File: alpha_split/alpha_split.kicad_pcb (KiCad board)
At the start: 2 copper layers, 109 x 71 mm, 154 parts, among them J1 USB_C_Receptacle, J2 USB_C_Receptacle, J3 PDI, J4 D4, J5 D5, J6 A6, J7 A7, J8 B0, J9 E2, K00 K00, K01 K01, K02 K02, K03 K03, K04 K04, K05 K05, K10 K10, K11 K11, K12 K12, K13 K13, K14 K14, K15 K15, K20 K20, K21 K21, K22 K22, K23 K23, K24 K24, K25 K25, K30 K30, K31 K31, K32 K32, K33 K33, K34 K34, K35 K35, SW1 Switch-6P-2S2T, SW2 RST_SW, U1 MCP73831, U2 MCP1700 (3.0V), U3 MCP1700 (3.3V), U4 ATXMEGA-A4U-EPAD, U5 74LVC1G34, U6 nRF24L01_module, U7 FSUSB42, U8 FSUSB42, U9 FSUSB42

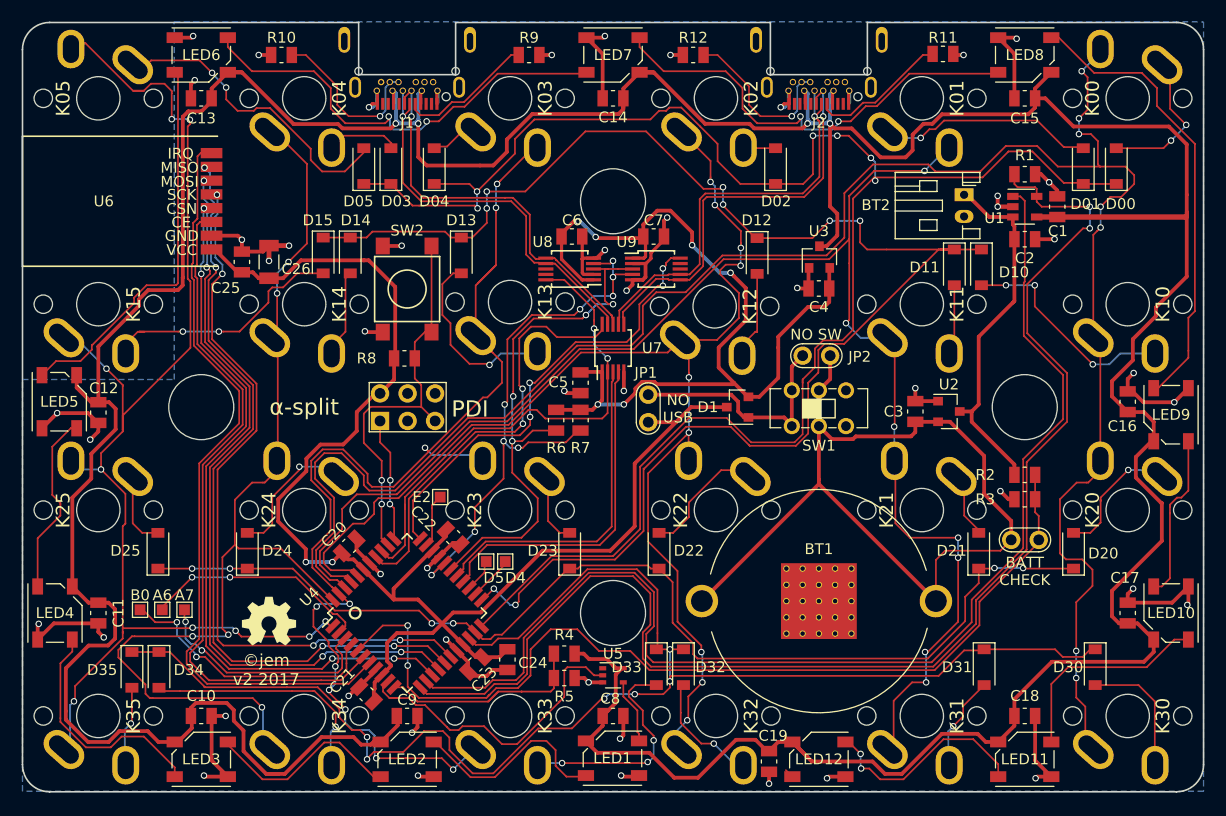
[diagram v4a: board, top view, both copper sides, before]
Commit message: updates for alpha split based on v2 prototype board
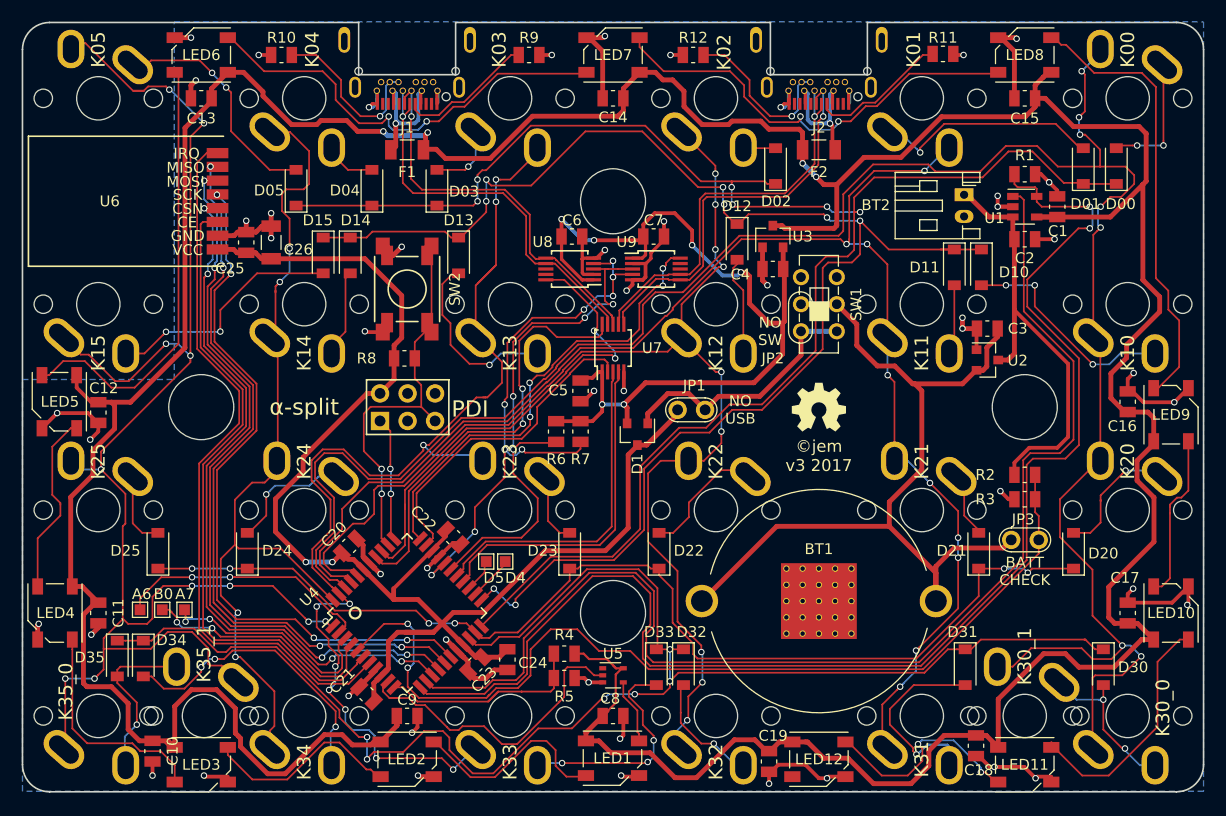
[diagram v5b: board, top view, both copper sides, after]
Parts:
- removed J9: E2, TestPoint:TestPoint_Pad_1.0x1.0mm
- added F1: Polyfuse, Resistor_SMD:R_1206_3216Metric, F.Cu at (35.5, 11.8)
- added F2: Polyfuse, Resistor_SMD:R_1206_3216Metric, F.Cu at (73.5, 11.8)
- added K30_1: K31, switch_mx:Cherry_MX_Matias_Slots_NoSilk_Back, B.Cu at (92.5, 64.0)
- added K35_1: K35, switch_mx:Cherry_MX_Matias_Slots_NoSilk_Back, B.Cu at (16.8, 64.0)
- SW2: value RST_SW -> SW_Push; footprint switch:SwitchPush_C&K_PTS645_SMT -> switch:SwitchPush_C&K_MultiFoot_RS-187R05A2-DS_And_PTS645_SMT
- moved svg2mod 54.5 mm to (73.5, 35.5)
- moved C3 10.1 mm to (89.0, 28.2), turned to 0 degrees
- moved SW1 9.60 mm to (73.5, 26.0), turned to 90 degrees
- moved D1 9.58 mm to (56.8, 38.0), turned to 270 degrees
- moved D05 6.56 mm to (25.2, 15.2)
- moved U2 5.93 mm to (89.0, 31.1)
- moved C10 5.55 mm to (12.0, 67.2), turned to 270 degrees
- moved JP1 5.43 mm to (63.0, 35.8), turned to 270 degrees
- moved C18 5.27 mm to (88.0, 66.8), turned to 270 degrees
- moved U3 4.70 mm to (69.2, 19.8)
- moved C4 4.62 mm to (69.2, 22.8)
- moved JP2 3.55 mm to (71.8, 28.5), turned to 180 degrees
- moved D04 2.66 mm to (32.2, 15.2)
- moved D12 2.26 mm to (66.0, 20.2)
- moved J6 2.05 mm to (10.8, 54.2)
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- renumbered K30 to K30_0, K35 to K35_0
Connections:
- J1 pad : Net-(J1-PadB5) -> (no net)
- J1 pad A4: +5V -> Net-(F1-Pad1)
- J1 pad A9: +5V -> Net-(F1-Pad1)
- J1 pad B4: +5V -> Net-(F1-Pad1)
- J1 pad B5: Net-(J1-PadB5) -> Net-(J1-PadB3)
- J1 pad B9: +5V -> Net-(F1-Pad1)
- J2 pad : Net-(J2-PadB5) -> (no net)
- J2 pad A4: +5V -> Net-(F2-Pad1)
- J2 pad A9: +5V -> Net-(F2-Pad1)
- J2 pad B4: +5V -> Net-(F2-Pad1)
- J2 pad B5: Net-(J2-PadB5) -> Net-(J2-PadB3)
- J2 pad B9: +5V -> Net-(F2-Pad1)
- R10 pad 1: Net-(J1-PadB5) -> Net-(J1-PadB3)
- R12 pad 1: Net-(J2-PadB5) -> Net-(J2-PadB3)
- SW2 pad 2: GND -> /RST
- U4 pad 32: /E2 -> /USB_SEL
- U7 pad 2: /I2C_LEFT -> /USB_SEL
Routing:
- net +5V: track 424.6 -> 278.5 mm, vias 4 -> 15
- net GND: track 173.2 -> 283.8 mm, vias 49 -> 40
- net /USB_SEL: track 0.00 -> 30.3 mm
- net /COL5: track 122.1 -> 147.7 mm, vias 9 -> 11
- net Net-(LED12-Pad2): track 0.85 -> 18.4 mm, vias 0 -> 2
- net Net-(LED10-Pad4): track 15.4 -> 32.5 mm
- net /COL0: track 188.6 -> 205.2 mm
- net Net-(J1-PadB5): track 16.0 -> 0.00 mm, vias 1 -> 0
- net Net-(J1-PadB3): track 0.00 -> 16.0 mm, vias 0 -> 1
- net Net-(J2-PadB5): track 15.8 -> 0.00 mm, vias 1 -> 0
- net Net-(J2-PadB3): track 0.00 -> 15.7 mm, vias 0 -> 1
- net Net-(LED2-Pad2): track 18.5 -> 34.0 mm
- net Net-(LED8-Pad2): track 42.6 -> 27.7 mm, vias 0 -> 1
- net Net-(LED7-Pad2): track 42.3 -> 27.6 mm, vias 2 -> 1
- net /COL4: track 97.5 -> 84.1 mm, vias 6 -> 4
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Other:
- net class Escape removed
- net class Power: trace_width 0.35 -> 0.45
- board text added: "NO SW"
- board text added: "©jem v3 2017"
- board text removed: "E2"
- board text removed: "©jem v2 2017"

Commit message: BAT_PROG signal not connected properly
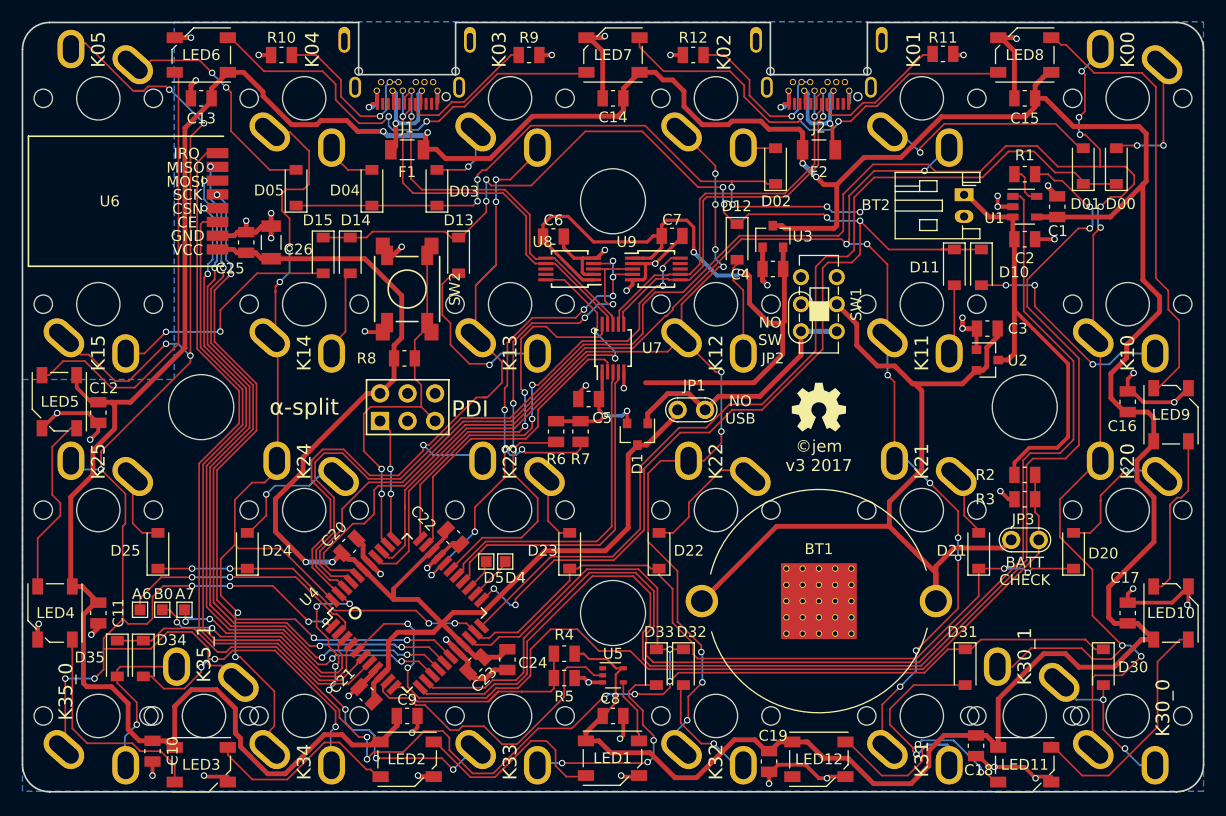
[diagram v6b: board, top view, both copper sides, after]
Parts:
- F1, F2: value Polyfuse -> Fuse
- K30_1: value K31 -> K30
- moved C6 1.70 mm to (49.0, 19.8)
- moved C7 1.70 mm to (60.0, 19.7)
- moved C5 1.06 mm to (52.2, 34.8), turned to 180 degrees
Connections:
- R1 pad 1: /BAT_PROG -> Net-(R1-Pad1)
- R1 pad 2: GND -> /BAT_PROG
- U1 pad 5: /BAT_PROG -> Net-(R1-Pad1)
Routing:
- net GND: track 283.8 -> 166.8 mm, vias 40 -> 51
- net +5V: track 278.5 -> 394.8 mm, vias 15 -> 4
- net Net-(LED12-Pad2): track 18.4 -> 0.00 mm, vias 2 -> 0
- net Net-(LED10-Pad4): track 32.5 -> 15.4 mm
- net Net-(LED2-Pad2): track 34.0 -> 18.7 mm
- net Net-(LED7-Pad2): track 27.6 -> 41.6 mm, vias 1 -> 2
- net Net-(LED8-Pad2): track 27.7 -> 41.4 mm, vias 1 -> 0
- net Net-(LED10-Pad2): track 10.6 -> 22.5 mm
- net Net-(LED3-Pad2): track 10.6 -> 20.6 mm
- net Net-(LED5-Pad2): track 31.8 -> 41.8 mm, vias 1 -> 0
- net Net-(LED6-Pad2): track 46.7 -> 42.3 mm, vias 1 -> 2
- net Net-(R1-Pad1): track 0.00 -> 3.89 mm
- net /BAT_PROG: track 126.0 -> 122.4 mm
- net Net-(LED1-Pad2): track 22.5 -> 19.1 mm
- net Net-(LED11-Pad2): track 21.7 -> 20.3 mm, vias 0 -> 2
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
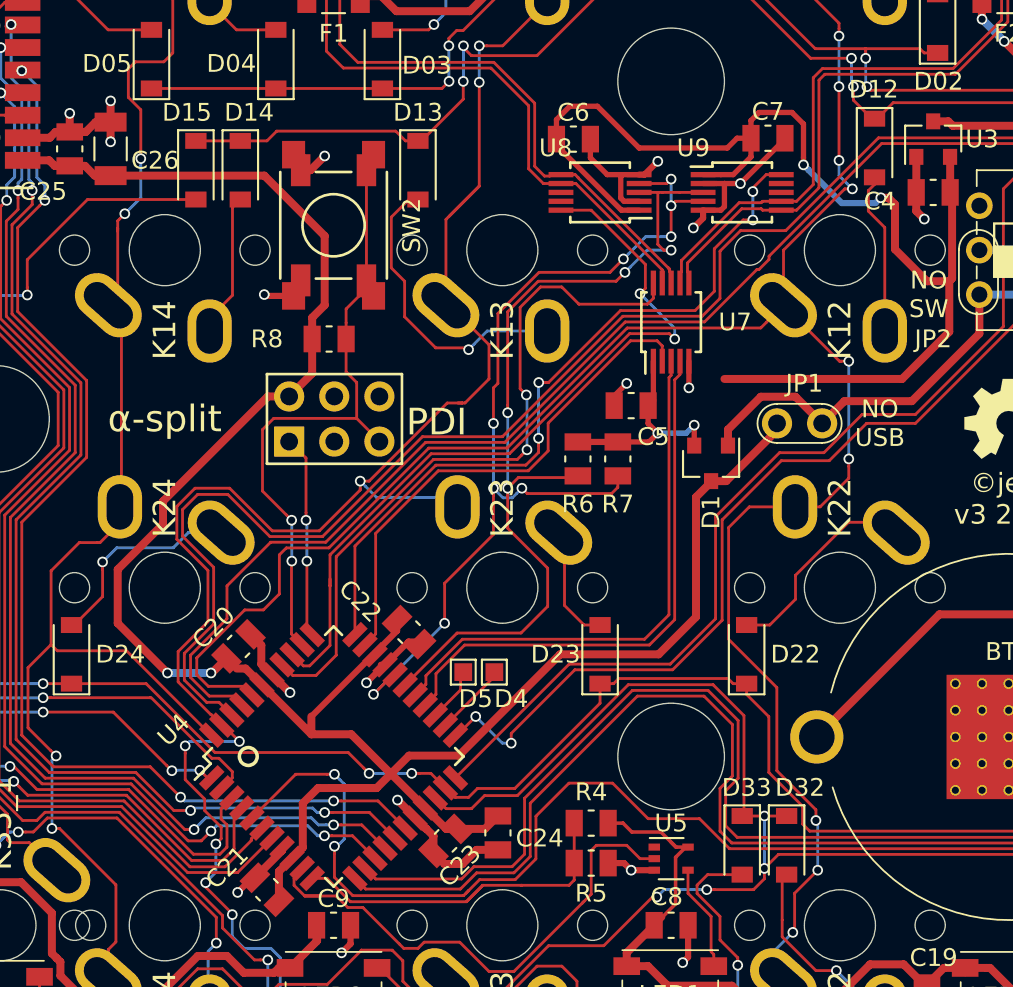
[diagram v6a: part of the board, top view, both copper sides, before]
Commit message: add Tag Connect programming header
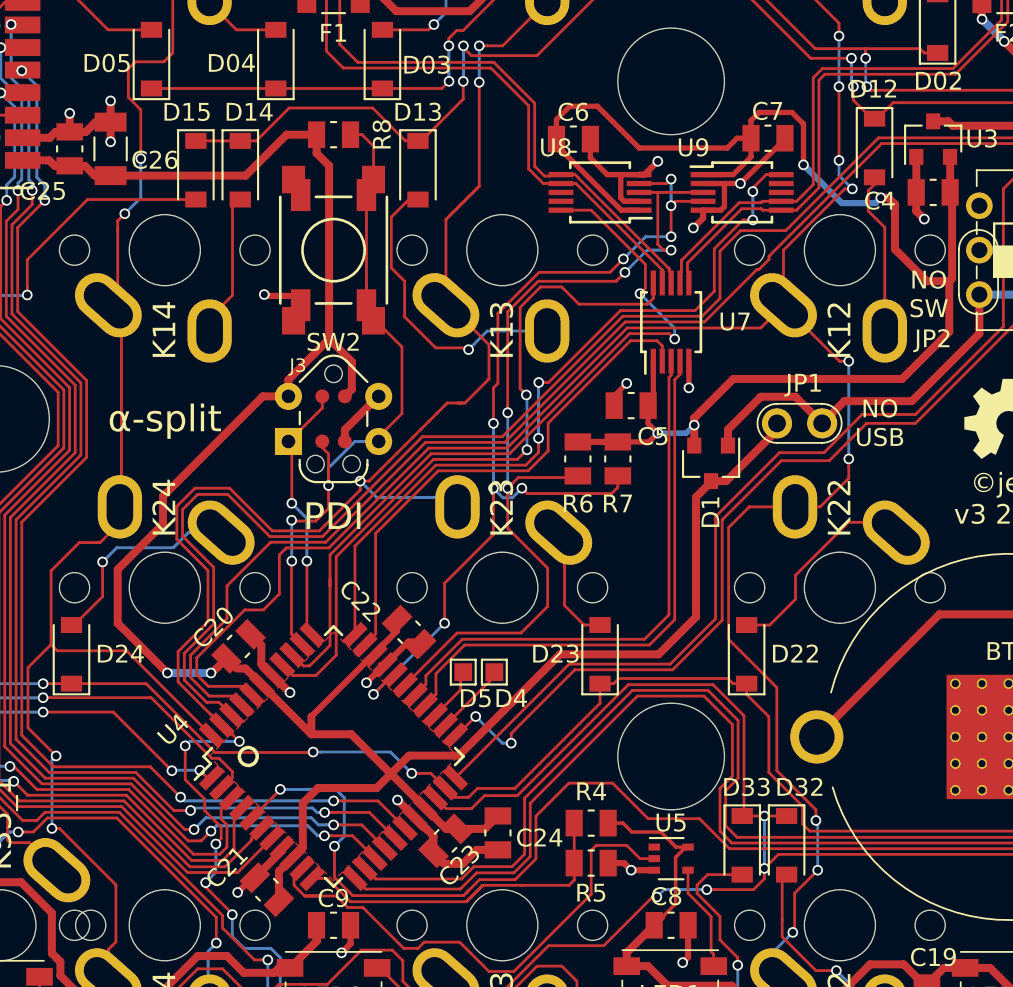
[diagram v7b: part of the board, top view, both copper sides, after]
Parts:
- J3: value PDI -> TC2030-IDC; footprint Conn_PinHeader_2.54mm:PinHeader_2x03_P2.54mm_Vertical -> Tag-Connect:TC2030-NL_SMALL_AND_IDC_PDI
- moved R8 11.5 mm to (35.5, 19.5)
- moved J3 2.81 mm to (35.5, 35.5), turned to 270 degrees
- moved SW2 1.40 mm to (35.5, 26.0)
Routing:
- net VCC: track 135.8 -> 141.1 mm
- net /PDI: track 11.5 -> 14.9 mm
- net +3V3: track 81.3 -> 84.4 mm
- net /RST: track 35.7 -> 38.3 mm, vias 2 -> 3
- net GND: track 166.8 -> 169.1 mm, vias 51 -> 50
- net /BAT_LVL: track 88.9 -> 87.7 mm
- net /ROW1: track 136.1 -> 137.2 mm
- added copper zone on F.Cu, net VCC

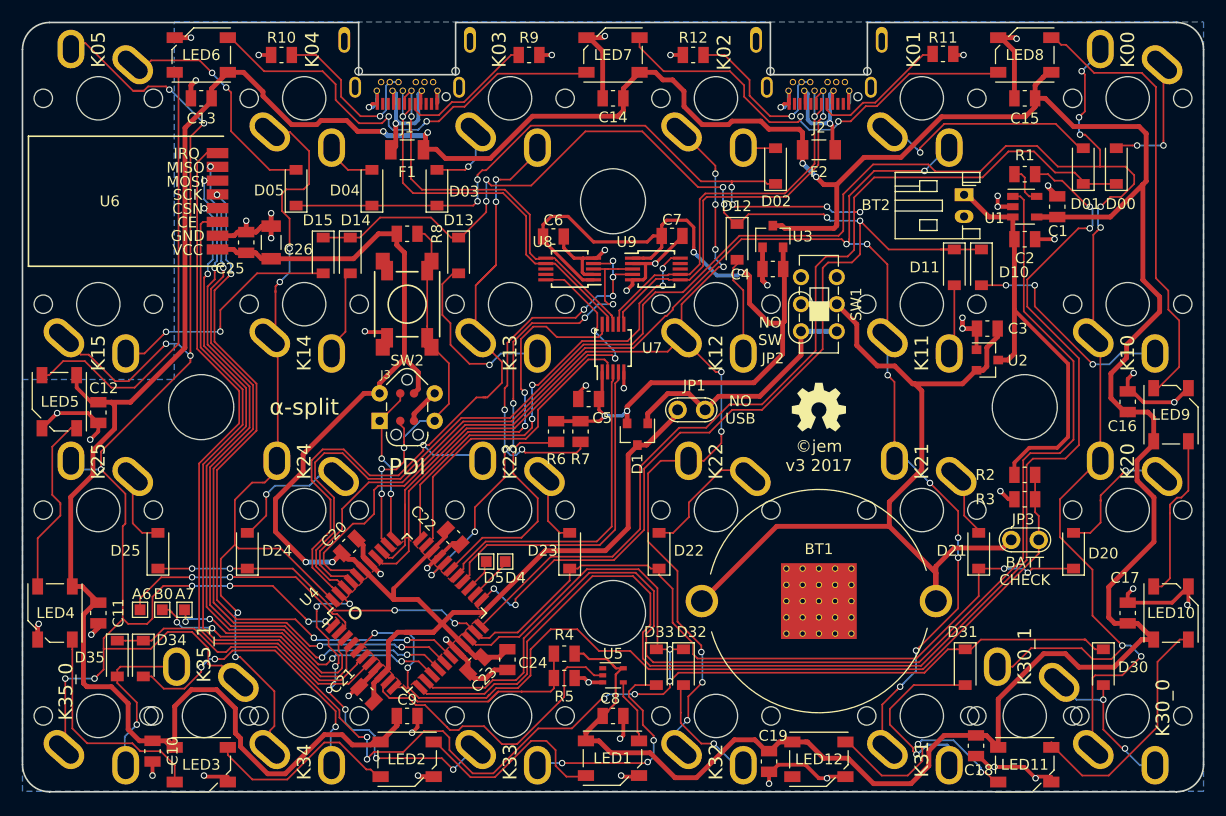
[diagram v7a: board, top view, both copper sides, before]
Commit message: give up on trying to support multiple switch layouts
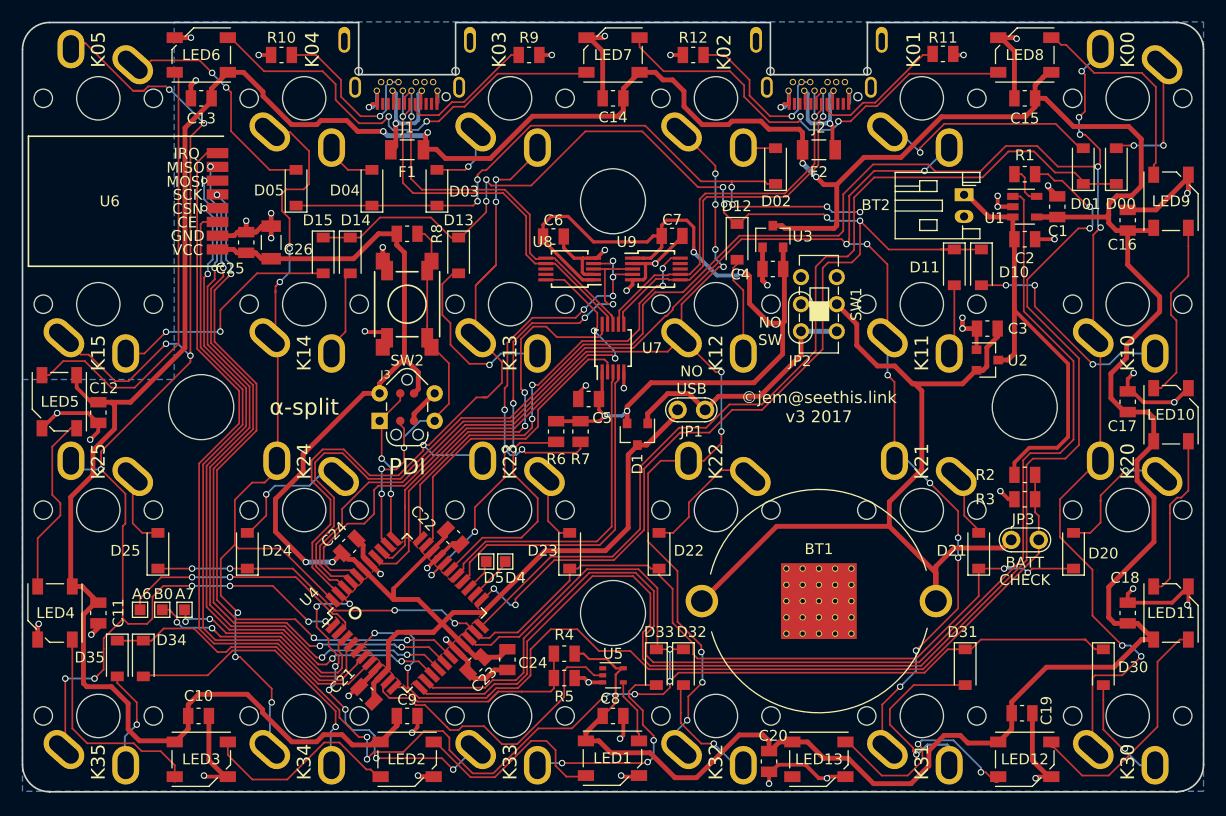
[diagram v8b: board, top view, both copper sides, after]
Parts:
- removed K30_1: K30, switch_mx:Cherry_MX_Matias_Slots_NoSilk_Back
- removed K35_1: K35, switch_mx:Cherry_MX_Matias_Slots_NoSilk_Back
- removed svg2mod: G***, logo:OSHW_5x5mm_SilkS
- added C16: 0.1uF, Capacitor_SMD:C_0805_2012Metric, F.Cu at (102.0, 18.2)
- added LED9: WS2812B, neopixel:WS2812B, F.Cu at (106.0, 16.5)
- C24: value 10uF -> 0.1uF
- C25: value 47uF -> 10uF
- moved C10 5.35 mm to (16.2, 64.0), turned to 0 degrees
- moved C19 5.20 mm to (92.2, 63.8), turned to 0 degrees
- moved LED12 0.50 mm to (92.5, 68.0)
- moved LED3 0.50 mm to (16.5, 68.0)
- renumbered C16 to C17, C17 to C18, C18 to C19, C19 to C20, C20 to C24, K30_0 to K30, K35_0 to K35, LED9 to LED10, LED10 to LED11, LED11 to LED12, LED12 to LED13
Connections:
- LED10 pad 4: Net-(LED8-Pad2) -> Net-(LED10-Pad4)
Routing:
- net Net-(LED8-Pad2): track 41.4 -> 19.7 mm
- net /COL0: track 205.1 -> 186.2 mm
- net Net-(LED10-Pad4): track 0.00 -> 17.4 mm
- net /COL5: track 147.7 -> 131.8 mm
- net GND: track 169.1 -> 184.7 mm
- net +5V: track 394.8 -> 385.9 mm
- net Net-(D35-Pad2): track 16.3 -> 10.1 mm
- net Net-(D30-Pad2): track 15.5 -> 10.4 mm, vias 2 -> 1
- net Net-(D34-Pad2): track 28.0 -> 26.8 mm, vias 3 -> 1
- net /COL4: track 84.1 -> 83.9 mm, vias 4 -> 5
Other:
- board text added: "©jem@seethis.link v3 2017"
- board text removed: "©jem v3 2017"
